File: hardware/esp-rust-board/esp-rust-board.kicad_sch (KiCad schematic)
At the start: 70 parts, among them J1 USB4105-GF-A, J2 GPIO, J3 POWER, J8 BATTERY, Q1 DMG3415U, Q4 MMBT3904, SW1 RESET, SW2 BOOT, SW3 SW_DPDT_x2, U1 SHTC3, U2 ICM-42670-P, U3 ESP32-C3-MINI-1, U4 Rust_Board, U5 SY8088, U6 MCP73831T-2ACI/OT, U7 MAX17048G_T10, U8 BMP280, U9 QMC5883L

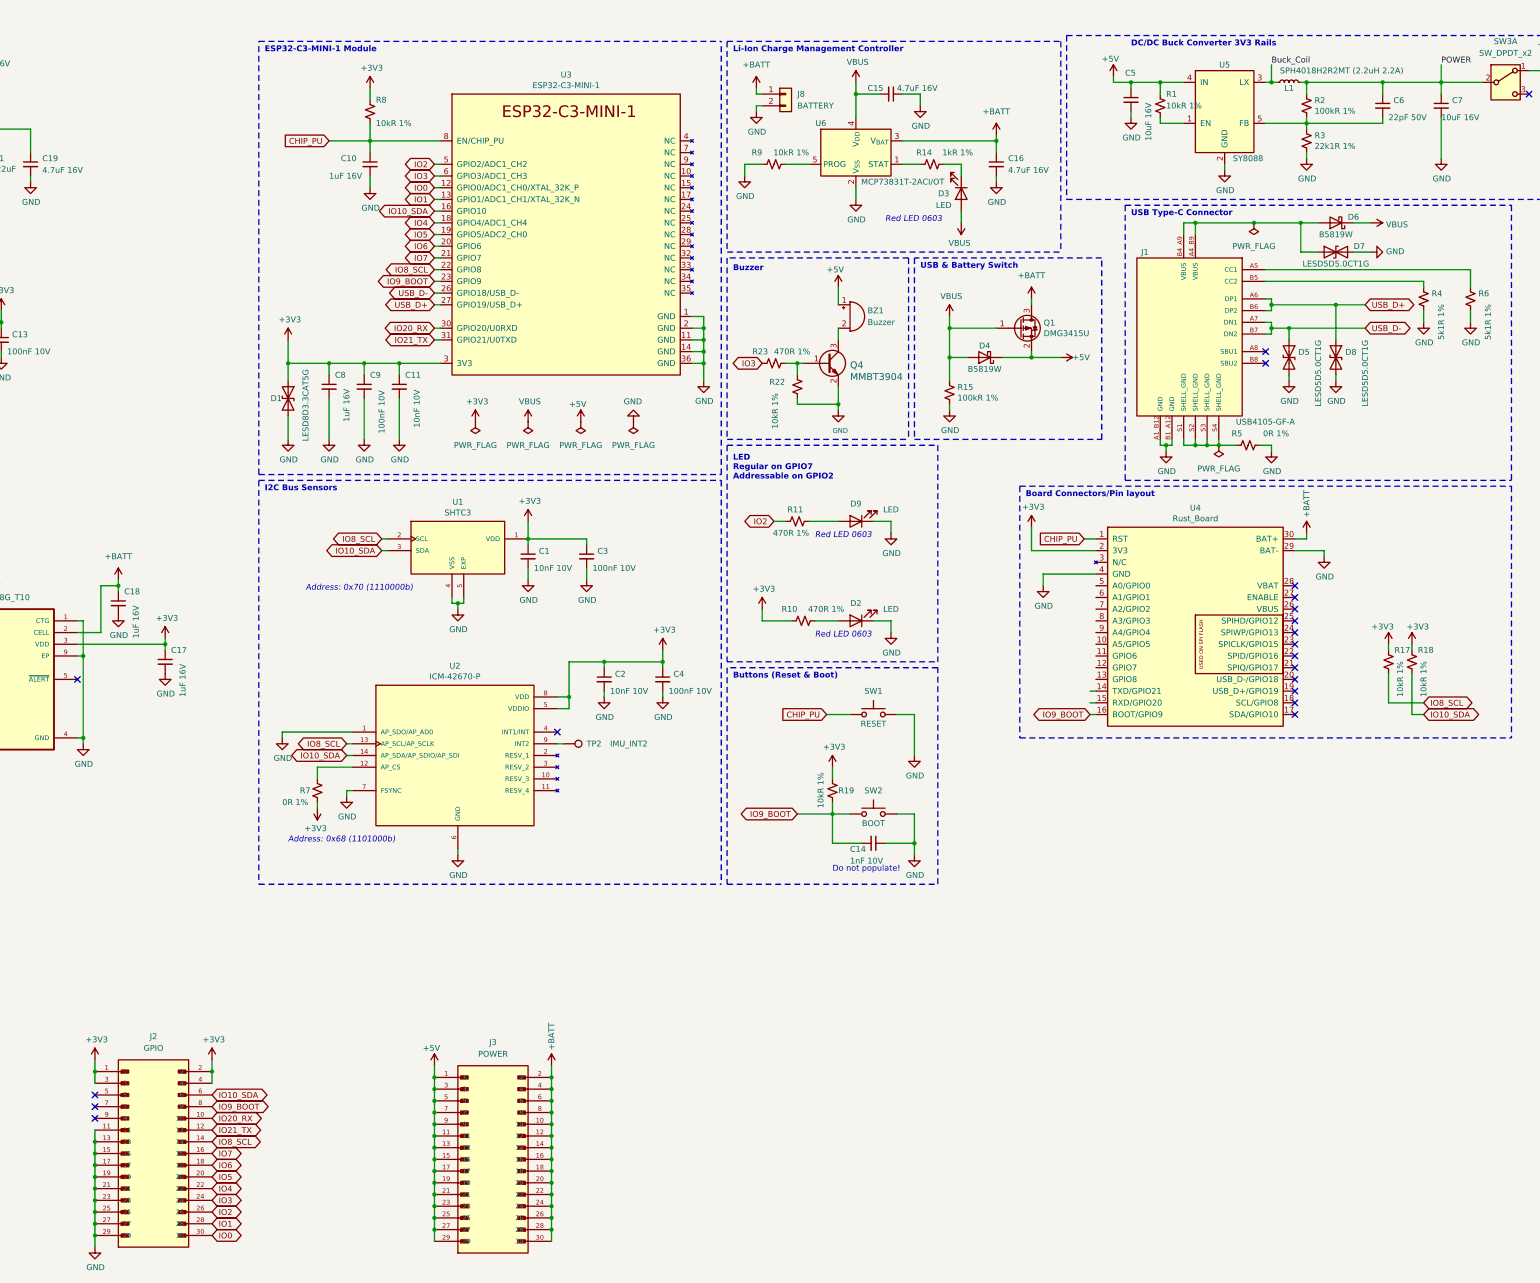
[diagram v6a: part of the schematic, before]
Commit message: Reorganize PCB, remove piezo, temperature sensor and expansion connections
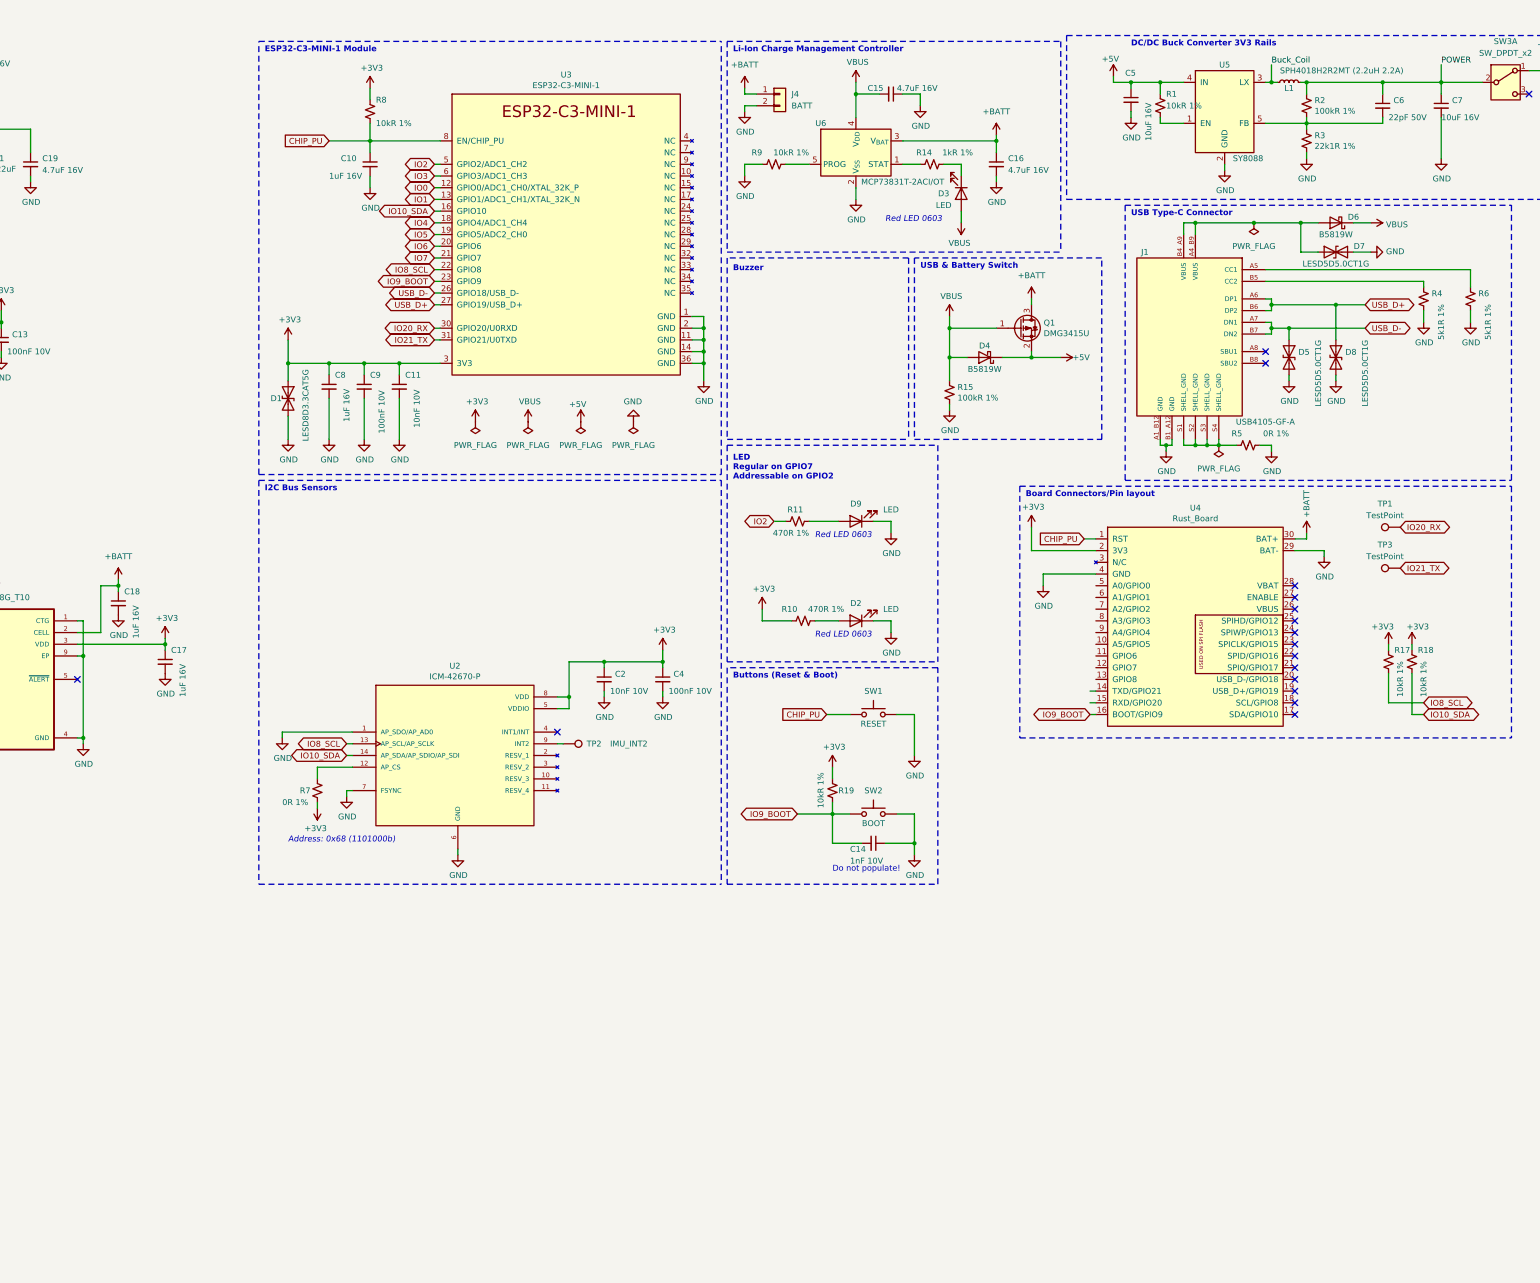
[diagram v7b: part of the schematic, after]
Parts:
- removed BZ1: Buzzer, Rust_Board:MLT-5020, symbol Device:Buzzer
- removed C1: 10nF 10V, Capacitor_SMD:C_0402_1005Metric, symbol Device:C_Small
- removed C3: 100nF 10V, Capacitor_SMD:C_0402_1005Metric, symbol Device:C_Small
- removed J2: GPIO, Rust_Board:HRS_DF37C-30DP-0.4V_51_, symbol DF37C-30DP-0.4V_51_:DF37C-30DP-0.4V_51_
- removed J3: POWER, Rust_Board:HRS_DF37C-30DP-0.4V_51_, symbol DF37C-30DP-0.4V_51_:DF37C-30DP-0.4V_51_
- removed J8: BATTERY, Connector_JST:JST_XH_B2B-XH-AM_1x02_P2.50mm_Vertical, symbol Connector_Generic:Conn_01x02
- removed Q4: MMBT3904, Package_TO_SOT_SMD:SOT-23, symbol Transistor_BJT:MMBT3904
- removed R22: 10kR 1%, Resistor_SMD:R_0402_1005Metric, symbol Device:R_Small_US
- removed R23: 470R 1%, Resistor_SMD:R_0402_1005Metric, symbol Device:R_Small_US
- removed U1: SHTC3, Sensor_Humidity:Sensirion_DFN-4-1EP_2x2mm_P1mm_EP0.7x1.6mm, symbol Rust_Board:SHTC3
- added J4: BATT, symbol Connector_Generic:Conn_01x02
- added TP1, TP3: TestPoint, TestPoint:TestPoint_Pad_D1.0mm, symbol Connector:TestPoint
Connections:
- net +BATT: now also J4.1 (Pin_1)
- net GND: now also J4.2 (Pin_2)
- net IO20_RX: now also TP1.1
- net IO21_TX: now also TP3.1
- no-connect marks 21 -> 18
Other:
- note removed: "Address: 0x70 (1110000b)"

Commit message: Add missing components
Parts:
- added C1, C3: 1uF, Capacitor_SMD:C_0402_1005Metric, symbol Device:C_Small
- added D10, D11: SS24, Diode_SMD:D_SOD-123, symbol Diode:SS24
- added J2: MOTOR L, Connector_JST:JST_PH_B2B-PH-SM4-TB_1x02-1MP_P2.00mm_Vertical, symbol Connector_Generic:Conn_01x02
- added J3: MOTOR R, Connector_JST:JST_PH_B2B-PH-SM4-TB_1x02-1MP_P2.00mm_Vertical, symbol Connector_Generic:Conn_01x02
- added J5: LED L, Connector_JST:JST_PH_B2B-PH-SM4-TB_1x02-1MP_P2.00mm_Vertical, symbol Connector_Generic:Conn_01x02
- added J6: LED R, Connector_JST:JST_PH_B2B-PH-SM4-TB_1x02-1MP_P2.00mm_Vertical, symbol Connector_Generic:Conn_01x02
- added Q2, Q3: Si2319CDS, Package_TO_SOT_SMD:SOT-23, symbol Transistor_FET:Si2319CDS
- added Q4, Q5: MMBT3904, Package_TO_SOT_SMD:SOT-23, symbol Transistor_BJT:MMBT3904
- added R13, R20, R22, R24: 470R 1%, Resistor_SMD:R_0402_1005Metric, symbol Device:R_Small_US
- added R16, R21, R23, R25: 10kR 1%, Resistor_SMD:R_0402_1005Metric, symbol Device:R_Small_US
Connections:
- net +BATT: now also C1.2, C3.2, D10.1 (K), D11.1 (K), J2.1 (Pin_1), J3.1 (Pin_1), J5.1 (Pin_1), J6.1 (Pin_1)
- net GND: now also Q2.2 (S), Q3.2 (S), Q4.2 (E), Q5.2 (E), R16.2, R21.2, R23.2, R25.2
- net IO0: now also R24.1
- net IO1: now also R22.1
- net IO6: now also R20.1
- net IO7: now also R13.1
- new net: Q3.1 (G), R20.2, R21.1
- new net: C1.1, D10.2 (A), J2.2 (Pin_2), Q2.3 (D)
- new net: C3.1, D11.2 (A), J3.2 (Pin_2), Q3.3 (D)
- new net: Q2.1 (G), R13.2, R16.1
- new net: Q5.1 (B), R24.2, R25.1
- new net: Q4.1 (B), R22.2, R23.1
- new net: J5.2 (Pin_2), Q4.3 (C)
- new net: J6.2 (Pin_2), Q5.3 (C)
